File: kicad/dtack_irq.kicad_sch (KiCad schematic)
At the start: 11 parts, among them U12 GAL22V10, U13 GAL22V10

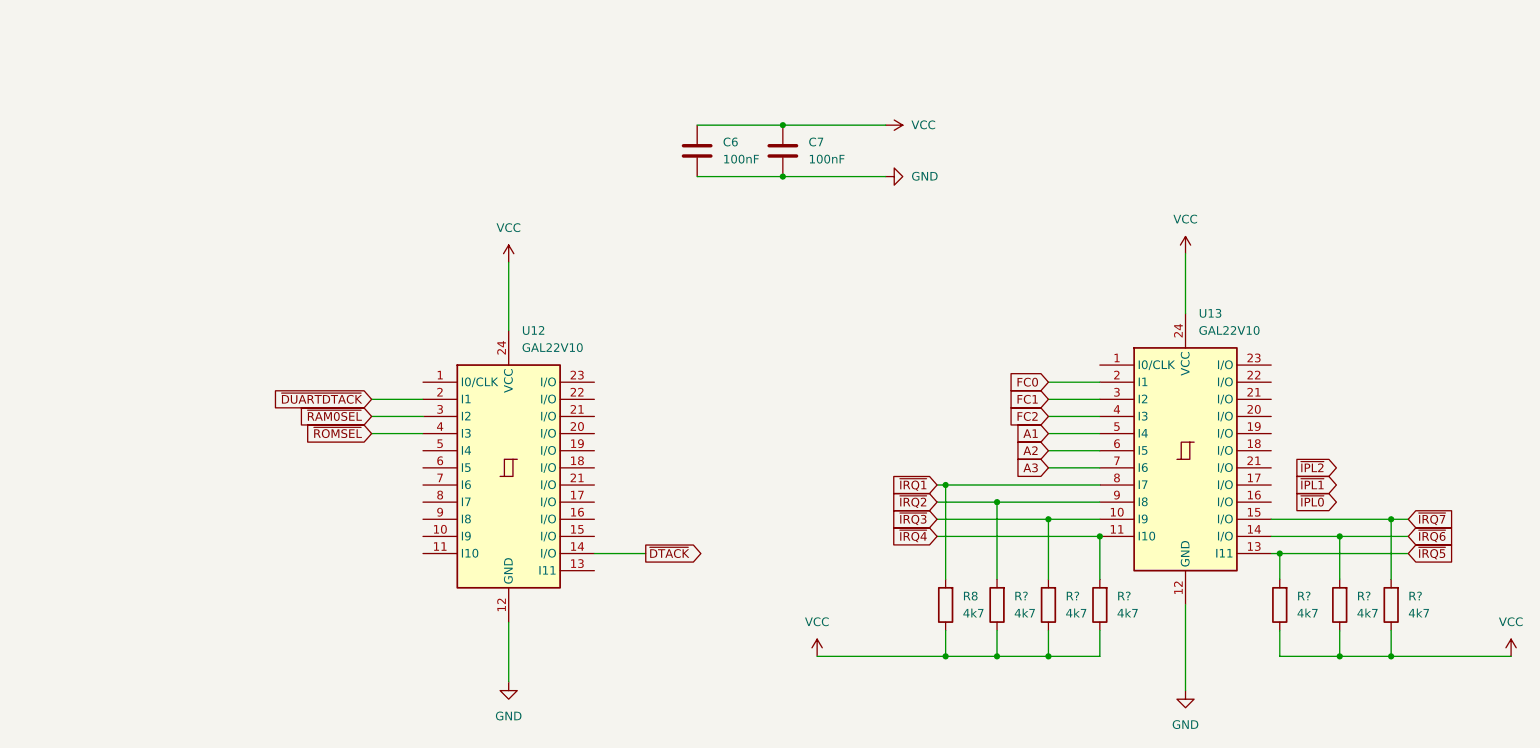
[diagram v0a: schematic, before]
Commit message: Revamped gluelogic for IRQ and DTACK
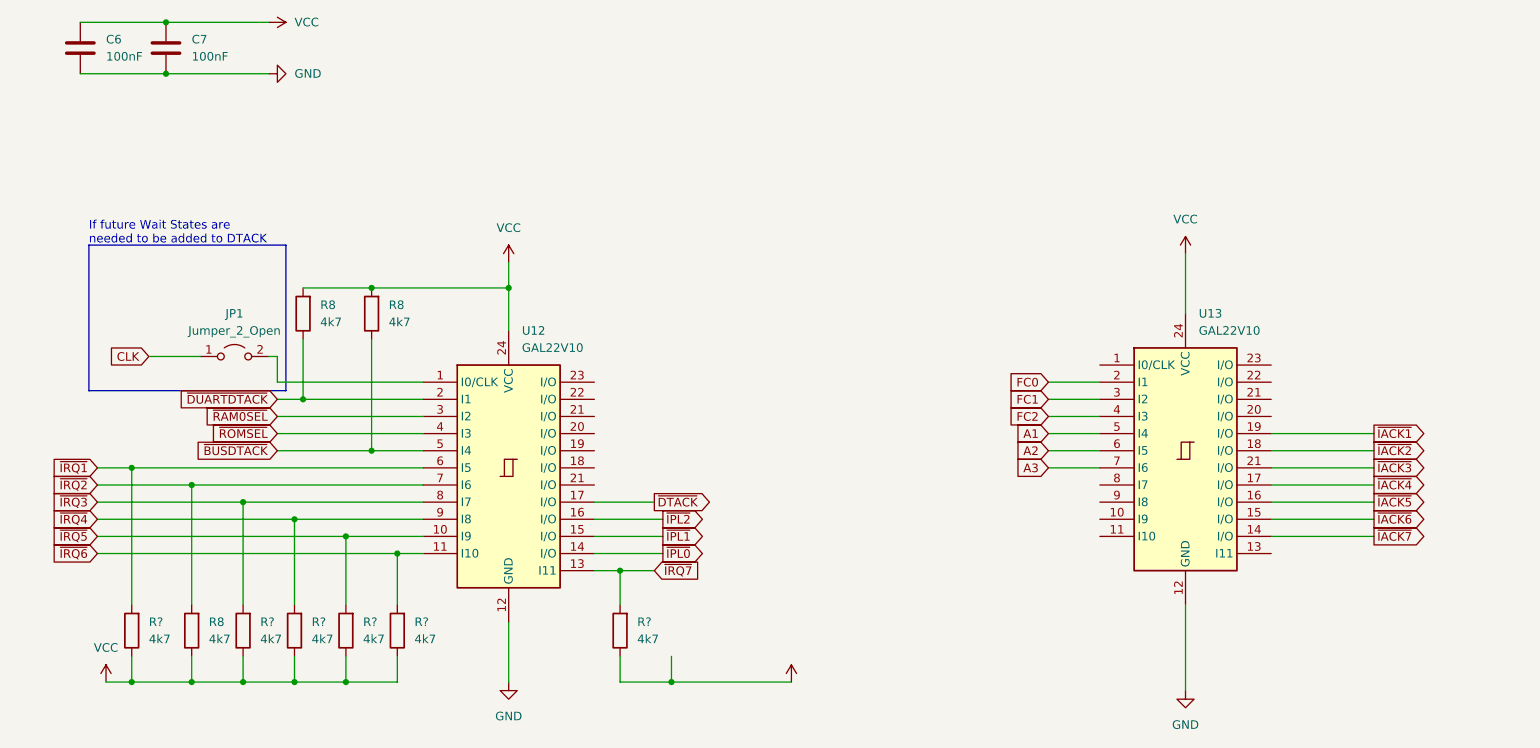
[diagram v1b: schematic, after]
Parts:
- removed R8, R? (x6): 4k7, Resistor_THT:R_Axial_DIN0207_L6.3mm_D2.5mm_P10.16mm_Horizontal, symbol Device:R
- added JP1: Jumper_2_Open, symbol Jumper:Jumper_2_Open
- added R8 (x3), R? (x6): 4k7, Resistor_THT:R_Axial_DIN0207_L6.3mm_D2.5mm_P10.16mm_Horizontal, symbol Device:R
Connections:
- net VCC: now also R8.1, R8.2, R8.2, R?.1, R?.1, R?.1, R?.1, R?.1, R?.1
- net ~{DTACK}: now also U12.17 (I/O); no longer U12.14 (I/O)
- net ~{DUARTDTACK}: now also R8.1
- net ~{IPL0}: now also U12.14 (I/O)
- net ~{IPL1}: now also U12.15 (I/O)
- net ~{IPL2}: now also U12.16 (I/O)
- net ~{IRQ1}: now also U12.6 (I5), R?.2; no longer U13.8 (I7)
- net ~{IRQ2}: now also U12.7 (I6), R8.2; no longer U13.9 (I8)
- net ~{IRQ3}: now also U12.8 (I7), R?.2; no longer U13.10 (I9)
- net ~{IRQ4}: now also U12.9 (I8), R?.2; no longer U13.11 (I10)
- net ~{IRQ5}: now also U12.10 (I9), R?.2; no longer U13.13 (I11)
- net ~{IRQ6}: now also U12.11 (I10), R?.2; no longer U13.14 (I/O)
- net ~{IRQ7}: now also U12.13 (I11), R?.2; no longer U13.15 (I/O)
- net at U12.1 (I0/CLK): now also JP1.2 (B)
- net ~{BUSDTACK}: now reaches U12.5 (I4)
- net ~{BUSDTACK}: now also R8.1
- net ~{IACK5}: now reaches U13.16 (I/O)
- net ~{IACK4}: now reaches U13.17 (I/O)
- net ~{IACK2}: now reaches U13.18 (I/O)
- net ~{IACK1}: now reaches U13.19 (I/O)
- net ~{IACK3}: now reaches U13.21 (I/O)
- new net CLK: JP1.1 (A)
- new net ~{IACK6}: U13.15 (I/O)
- new net ~{IACK7}: U13.14 (I/O)
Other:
- note added: "If future Wait States are needed to be added to DTACK"
- moved on the sheet: C6, C7
